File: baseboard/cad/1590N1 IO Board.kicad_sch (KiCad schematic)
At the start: 0 parts

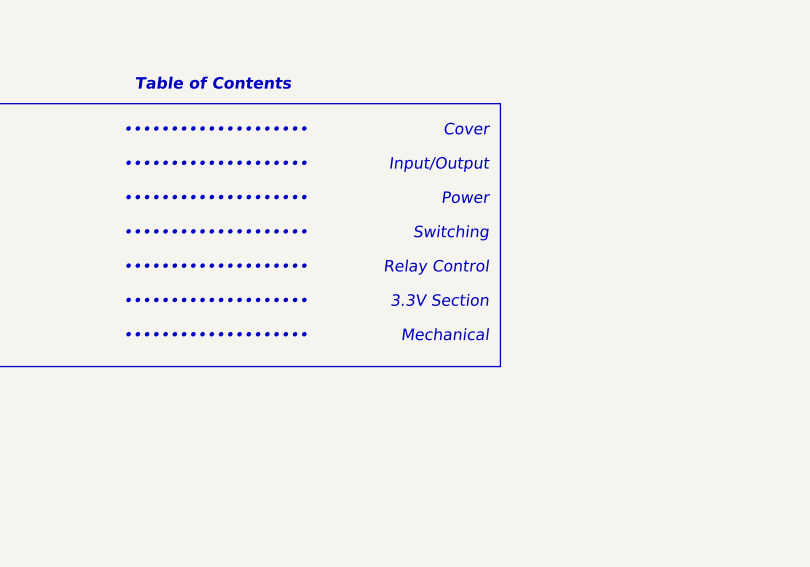
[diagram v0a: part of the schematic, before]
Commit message: added microcontroller enable to analog power rails
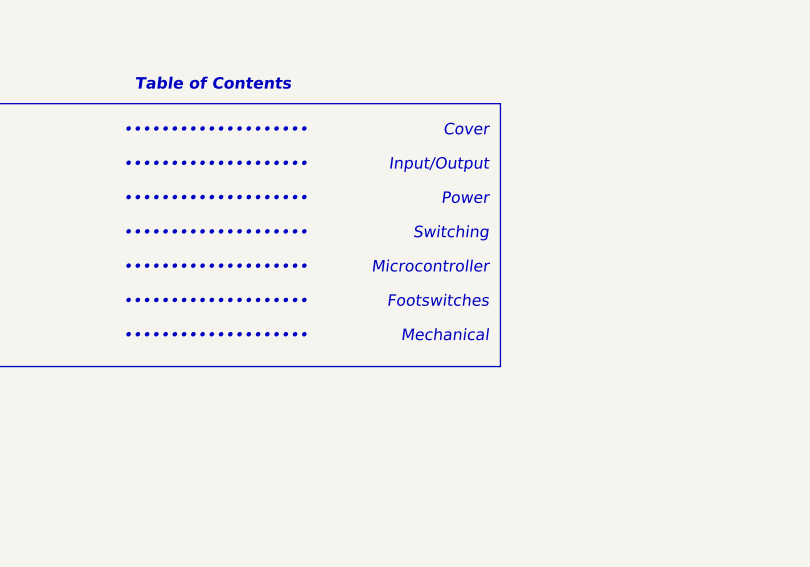
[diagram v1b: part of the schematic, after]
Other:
- note added: "Footswitches"
- note added: "Microcontroller"
- note removed: "3.3V Section"
- note removed: "Relay Control"
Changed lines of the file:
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@@
     (effects (font (size 1.27 1.27) italic) (justify left bottom))
   )
-  (text "3.3V Section" (at 171.45 116.84 0)
+  (text "Footswitches" (at 171.45 116.84 0)
     (effects (font (size 1.27 1.27) italic) (justify right bottom))
   )
-  (text "Relay Control\n" (at 171.45 113.03 0)
+  (text "Microcontroller" (at 171.45 113.03 0)
     (effects (font (size 1.27 1.27) italic) (justify right bottom))
   )

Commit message: added reset button to microcontroller
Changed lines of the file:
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@@
     (comment 9 "5: PCB LAYOUT ACCORDING TO DATASHEET FOR ALL COMPONENTS")
   )
-  (polyline (pts (xy 109.22 123.19) (xy 172.72 123.19))
+  (rectangle (start 109.22 93.98) (end 172.72 123.19)
     (stroke (width 0) (type default))
-  )
-  (polyline (pts (xy 109.22 93.98) (xy 172.72 93.98))
-    (stroke (width 0) (type default))
-  )
-  (polyline (pts (xy 172.72 123.19) (xy 172.72 93.98))
-    (stroke (width 0) (type default))
-  )
-  (polyline (pts (xy 109.22 93.98) (xy 109.22 123.19))
-    (stroke (width 0) (type default))
+    (fill (type none))
   )
   (text "••••••••••••••••••••" (at 130.81 116.84 0)

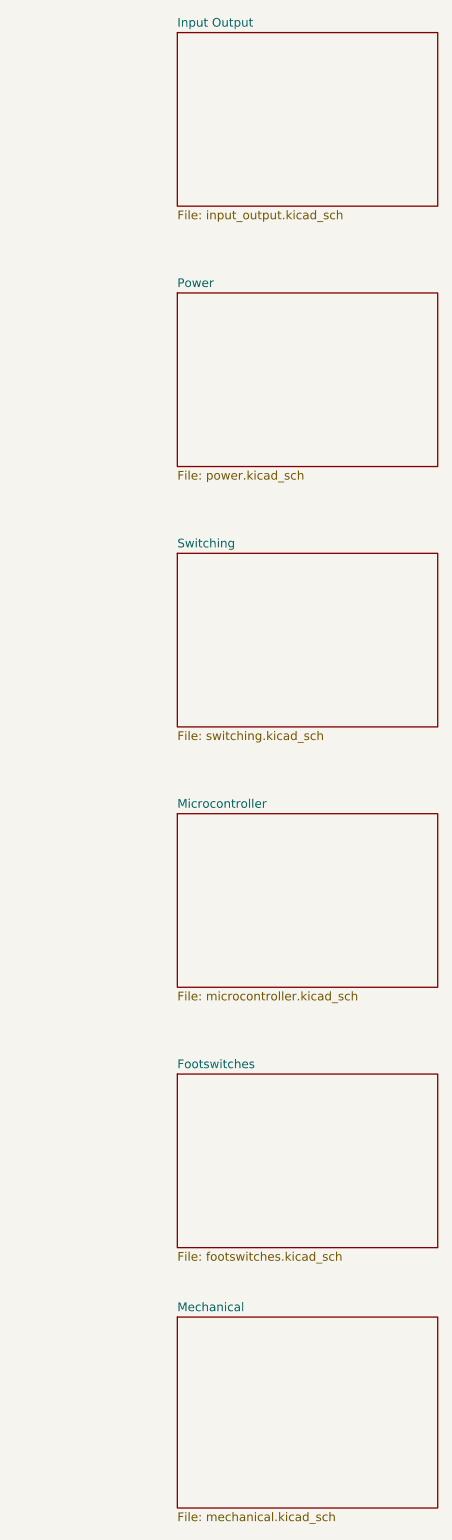
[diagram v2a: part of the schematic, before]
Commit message: swapped relays for nice analog switch, saved $4
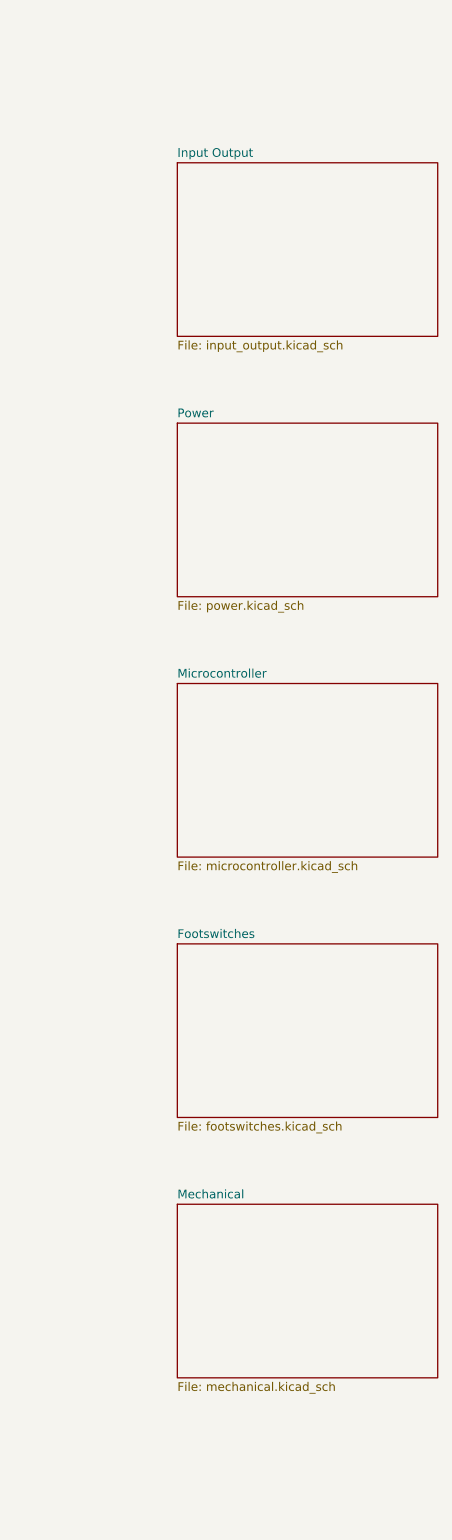
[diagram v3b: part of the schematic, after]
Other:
- removed sheet Switching
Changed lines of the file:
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@@
     (effects (font (size 1.27 1.27) italic) (justify left bottom))
   )
-  (sheet (at 304.8 114.3) (size 38.1 25.4) (fields_autoplaced)
+  (sheet (at 304.8 95.25) (size 38.1 25.4) (fields_autoplaced)
     (stroke (width 0.1524) (type solid))
     (fill (color 0 0 0 0.0000))
-    (property "Sheetname" "Microcontroller" (at 304.8 113.5884 0)
+    (property "Sheetname" "Microcontroller" (at 304.8 94.5384 0)
       (effects (font (size 1.27 1.27)) (justify left bottom))
     )
-    (property "Sheetfile" "microcontroller.kicad_sch" (at 304.8 140.2846 0)
+    (property "Sheetfile" "microcontroller.kicad_sch" (at 304.8 121.2346 0)
       (effects (font (size 1.27 1.27)) (justify left top))
     )
     (instances
       (project "1590N1 IO Board"
-        (path "/190888c1-6ce2-4681-a836-dc477e444e49" (page "7"))
+        (path "/190888c1-6ce2-4681-a836-dc477e444e49" (page "4"))
       )
     )
   )
-  (sheet (at 304.8 38.1) (size 38.1 25.4) (fields_autoplaced)
+  (sheet (at 304.8 57.15) (size 38.1 25.4) (fields_autoplaced)
     (stroke (width 0.1524) (type solid))
     (fill (color 0 0 0 0.0000))
-    (property "Sheetname" "Power" (at 304.8 37.3884 0)
+    (property "Sheetname" "Power" (at 304.8 56.4384 0)
       (effects (font (size 1.27 1.27)) (justify left bottom))
     )
-    (property "Sheetfile" "power.kicad_sch" (at 304.8 64.0846 0)
+    (property "Sheetfile" "power.kicad_sch" (at 304.8 83.1346 0)
       (effects (font (size 1.27 1.27)) (justify left top))
     )
@@
     )
   )
-  (sheet (at 304.8 187.96) (size 38.1 27.94) (fields_autoplaced)
+  (sheet (at 304.8 171.45) (size 38.1 25.4) (fields_autoplaced)
     (stroke (width 0.1524) (type solid))
     (fill (color 0 0 0 0.0000))
-    (property "Sheetname" "Mechanical" (at 304.8 187.2484 0)
+    (property "Sheetname" "Mechanical" (at 304.8 170.7384 0)
       (effects (font (size 1.27 1.27)) (justify left bottom))
     )
-    (property "Sheetfile" "mechanical.kicad_sch" (at 304.8 216.4846 0)
+    (property "Sheetfile" "mechanical.kicad_sch" (at 304.8 197.4346 0)
       (effects (font (size 1.27 1.27)) (justify left top))
-    )
-    (instances
-      (project "1590N1 IO Board"
-        (path "/190888c1-6ce2-4681-a836-dc477e444e49" (page "7"))
-      )
-    )
-  )
-  (sheet (at 304.8 152.4) (size 38.1 25.4) (fields_autoplaced)
-    (stroke (width 0.1524) (type solid))
-    (fill (color 0 0 0 0.0000))
-    (property "Sheetname" "Footswitches" (at 304.8 151.6884 0)
-      (effects (font (size 1.27 1.27)) (justify left bottom))
-    )
-    (property "Sheetfile" "footswitches.kicad_sch" (at 304.8 178.3846 0)
-      (effects (font (size 1.27 1.27)) (justify left top))
-    )
-    (property "Field2" "" (at 304.8 152.4 0)
-      (effects (font (size 1.27 1.27)) hide)
     )
     (instances
@@
     )
   )
-  (sheet (at 304.8 76.2) (size 38.1 25.4) (fields_autoplaced)
+  (sheet (at 304.8 133.35) (size 38.1 25.4) (fields_autoplaced)
     (stroke (width 0.1524) (type solid))
     (fill (color 0 0 0 0.0000))
-    (property "Sheetname" "Switching" (at 304.8 75.4884 0)
+    (property "Sheetname" "Footswitches" (at 304.8 132.6384 0)
       (effects (font (size 1.27 1.27)) (justify left bottom))
     )
-    (property "Sheetfile" "switching.kicad_sch" (at 304.8 102.1846 0)
+    (property "Sheetfile" "footswitches.kicad_sch" (at 304.8 159.3346 0)
       (effects (font (size 1.27 1.27)) (justify left top))
+    )
+    (property "Field2" "" (at 304.8 133.35 0)
+      (effects (font (size 1.27 1.27)) hide)
     )
     (instances
       (project "1590N1 IO Board"
-        (path "/190888c1-6ce2-4681-a836-dc477e444e49" (page "4"))
+        (path "/190888c1-6ce2-4681-a836-dc477e444e49" (page "5"))
       )
     )
   )
-  (sheet (at 304.8 0) (size 38.1 25.4) (fields_autoplaced)
+  (sheet (at 304.8 19.05) (size 38.1 25.4) (fields_autoplaced)
     (stroke (width 0.1524) (type solid))
     (fill (color 0 0 0 0.0000))
-    (property "Sheetname" "Input Output" (at 304.8 -0.7116 0)
+    (property "Sheetname" "Input Output" (at 304.8 18.3384 0)
       (effects (font (size 1.27 1.27)) (justify left bottom))
     )
-    (property "Sheetfile" "input_output.kicad_sch" (at 304.8 25.9846 0)
+    (property "Sheetfile" "input_output.kicad_sch" (at 304.8 45.0346 0)
       (effects (font (size 1.27 1.27)) (justify left top))
     )

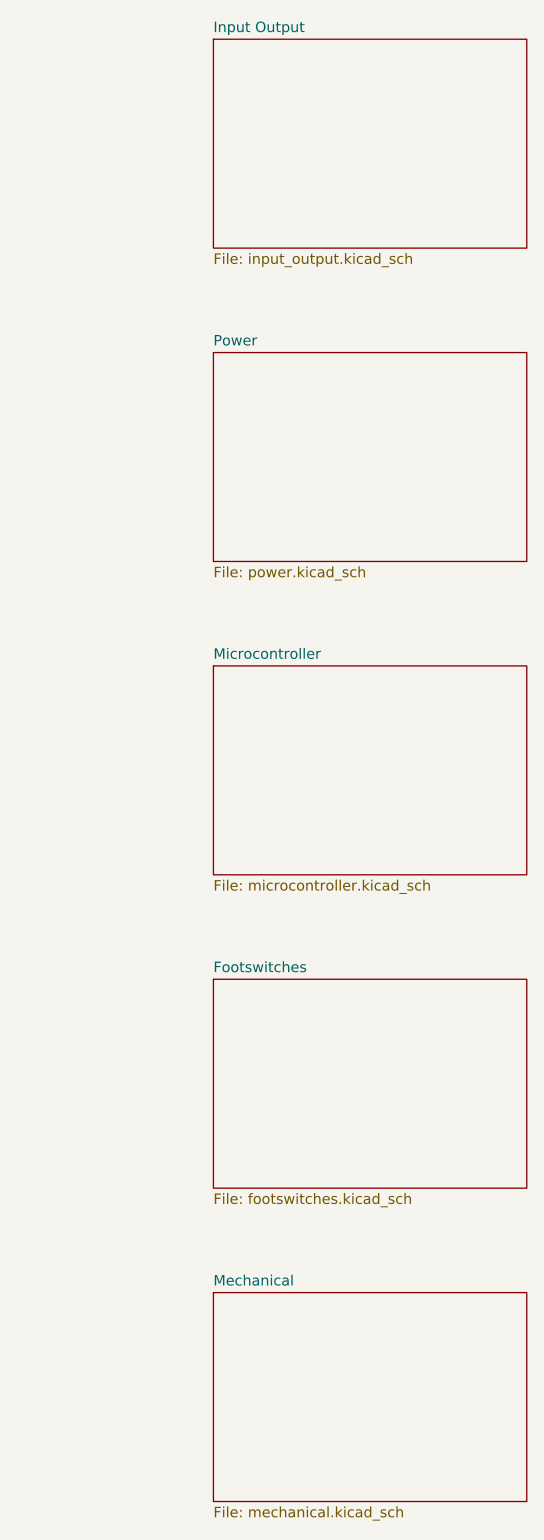
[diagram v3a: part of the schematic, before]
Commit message: updated schematic page setup
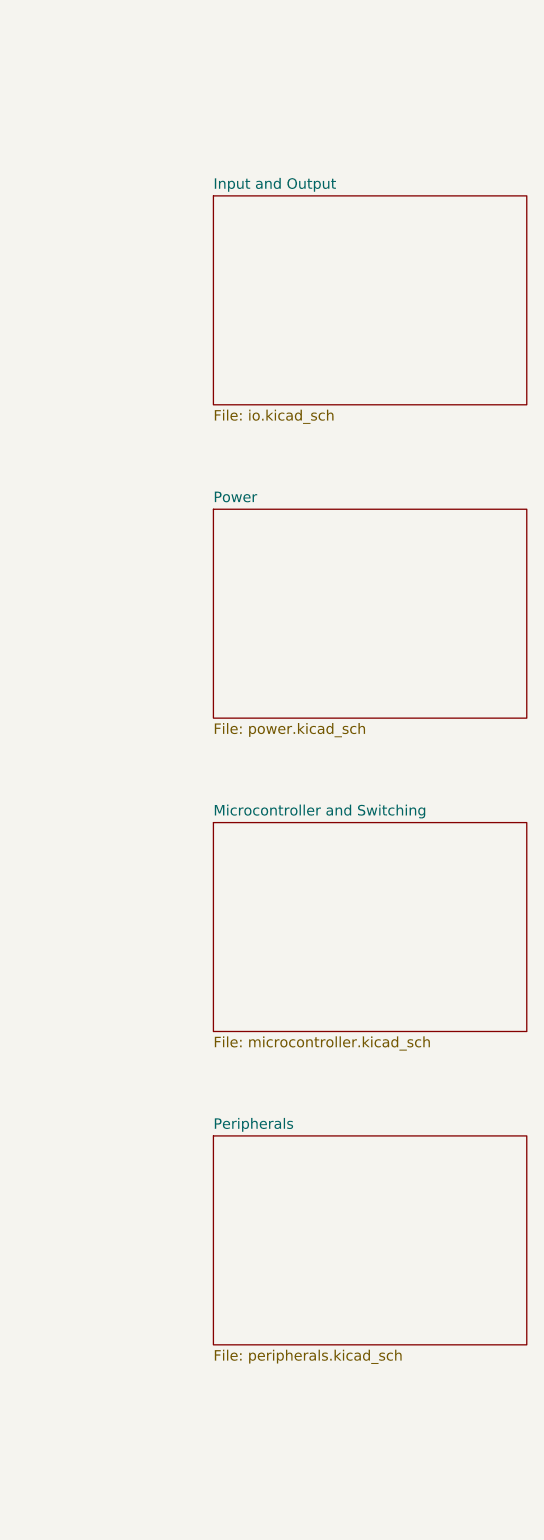
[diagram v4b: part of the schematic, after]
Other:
- sheet Footswitches renamed Peripherals
- sheet Input Output renamed Input and Output
- sheet Microcontroller renamed Microcontroller and Switching
- removed sheet Mechanical
- sheet Input and Output: file input_output.kicad_sch -> io.kicad_sch
- sheet Peripherals: file footswitches.kicad_sch -> peripherals.kicad_sch
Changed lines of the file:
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@@
     (effects (font (size 1.27 1.27) italic) (justify left bottom))
   )
-  (sheet (at 304.8 95.25) (size 38.1 25.4) (fields_autoplaced)
+  (sheet (at 304.8 114.3) (size 38.1 25.4) (fields_autoplaced)
     (stroke (width 0.1524) (type solid))
     (fill (color 0 0 0 0.0000))
-    (property "Sheetname" "Microcontroller" (at 304.8 94.5384 0)
+    (property "Sheetname" "Microcontroller and Switching" (at 304.8 113.5884 0)
       (effects (font (size 1.27 1.27)) (justify left bottom))
     )
-    (property "Sheetfile" "microcontroller.kicad_sch" (at 304.8 121.2346 0)
+    (property "Sheetfile" "microcontroller.kicad_sch" (at 304.8 140.2846 0)
       (effects (font (size 1.27 1.27)) (justify left top))
     )
@@
     )
   )
-  (sheet (at 304.8 57.15) (size 38.1 25.4) (fields_autoplaced)
+  (sheet (at 304.8 76.2) (size 38.1 25.4) (fields_autoplaced)
     (stroke (width 0.1524) (type solid))
     (fill (color 0 0 0 0.0000))
-    (property "Sheetname" "Power" (at 304.8 56.4384 0)
+    (property "Sheetname" "Power" (at 304.8 75.4884 0)
       (effects (font (size 1.27 1.27)) (justify left bottom))
     )
-    (property "Sheetfile" "power.kicad_sch" (at 304.8 83.1346 0)
+    (property "Sheetfile" "power.kicad_sch" (at 304.8 102.1846 0)
       (effects (font (size 1.27 1.27)) (justify left top))
     )
@@
     )
   )
-  (sheet (at 304.8 171.45) (size 38.1 25.4) (fields_autoplaced)
+  (sheet (at 304.8 152.4) (size 38.1 25.4) (fields_autoplaced)
     (stroke (width 0.1524) (type solid))
     (fill (color 0 0 0 0.0000))
-    (property "Sheetname" "Mechanical" (at 304.8 170.7384 0)
+    (property "Sheetname" "Peripherals" (at 304.8 151.6884 0)
       (effects (font (size 1.27 1.27)) (justify left bottom))
     )
-    (property "Sheetfile" "mechanical.kicad_sch" (at 304.8 197.4346 0)
+    (property "Sheetfile" "peripherals.kicad_sch" (at 304.8 178.3846 0)
       (effects (font (size 1.27 1.27)) (justify left top))
     )
-    (instances
-      (project "1590N1 IO Board"
-        (path "/190888c1-6ce2-4681-a836-dc477e444e49" (page "6"))
-      )
-    )
-  )
-  (sheet (at 304.8 133.35) (size 38.1 25.4) (fields_autoplaced)
-    (stroke (width 0.1524) (type solid))
-    (fill (color 0 0 0 0.0000))
-    (property "Sheetname" "Footswitches" (at 304.8 132.6384 0)
-      (effects (font (size 1.27 1.27)) (justify left bottom))
-    )
-    (property "Sheetfile" "footswitches.kicad_sch" (at 304.8 159.3346 0)
-      (effects (font (size 1.27 1.27)) (justify left top))
-    )
-    (property "Field2" "" (at 304.8 133.35 0)
+    (property "Field2" "" (at 304.8 152.4 0)
       (effects (font (size 1.27 1.27)) hide)
     )
@@
     )
   )
-  (sheet (at 304.8 19.05) (size 38.1 25.4) (fields_autoplaced)
+  (sheet (at 304.8 38.1) (size 38.1 25.4) (fields_autoplaced)
     (stroke (width 0.1524) (type solid))
     (fill (color 0 0 0 0.0000))
-    (property "Sheetname" "Input Output" (at 304.8 18.3384 0)
+    (property "Sheetname" "Input and Output" (at 304.8 37.3884 0)
       (effects (font (size 1.27 1.27)) (justify left bottom))
     )
-    (property "Sheetfile" "input_output.kicad_sch" (at 304.8 45.0346 0)
+    (property "Sheetfile" "io.kicad_sch" (at 304.8 64.0846 0)
       (effects (font (size 1.27 1.27)) (justify left top))
     )
